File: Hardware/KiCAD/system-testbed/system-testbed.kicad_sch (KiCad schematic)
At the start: 0 parts

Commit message: Update-Jumper-Schematic
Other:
- sheet Audio Subsystem renamed Audio Subsystem (TQFN)
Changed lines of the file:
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@@
 			(color 255 229 191 1.0000)
 		)
-		(property "Sheetname" "Audio Subsystem"
+		(property "Sheetname" "Audio Subsystem (TQFN)"
 			(at 204.47 45.0084 0)
 			(effects

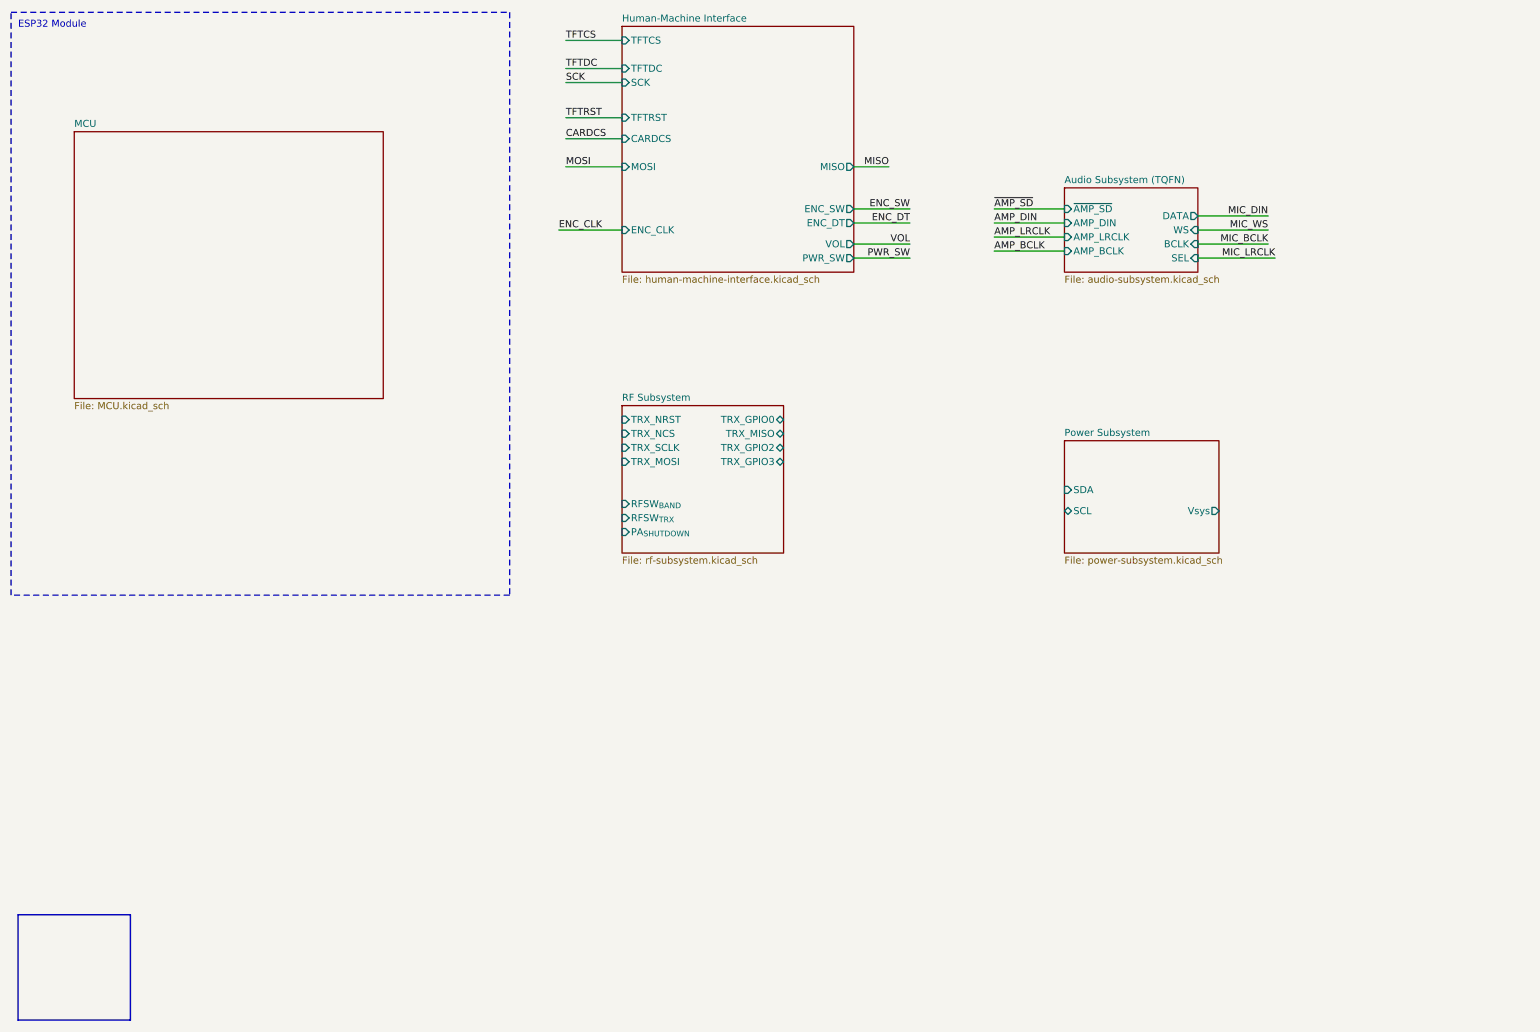
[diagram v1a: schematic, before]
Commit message: fix: clarify labellng and pin head #32
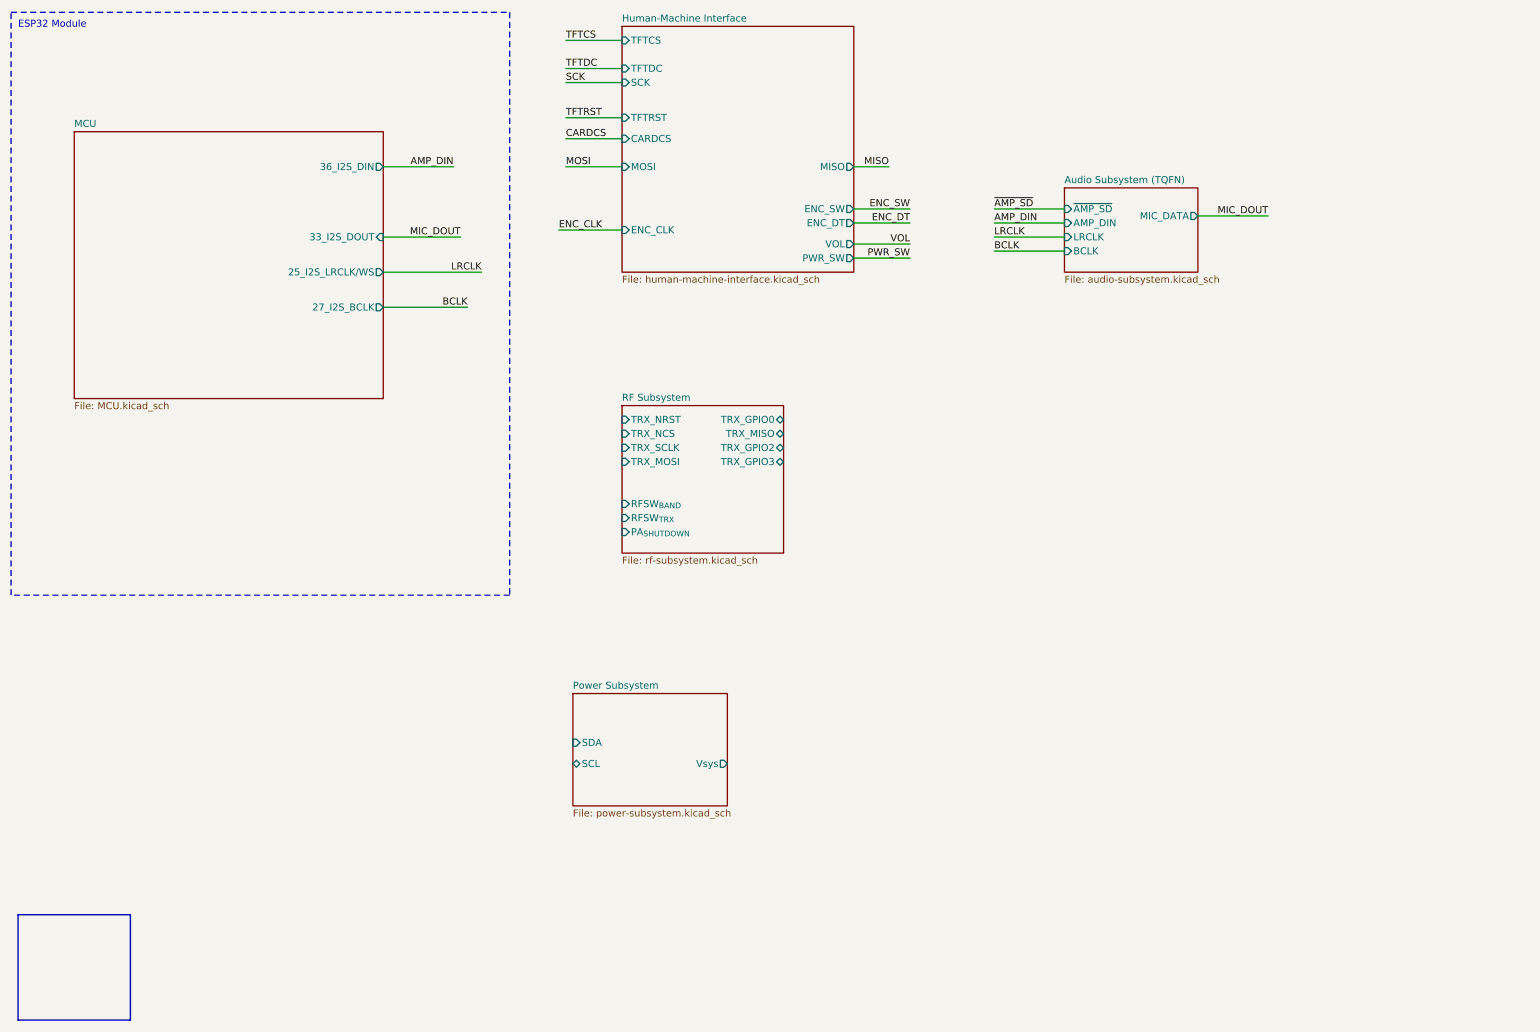
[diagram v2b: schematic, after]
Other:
- sheet Audio Subsystem (TQFN) ports: added LRCLK, MIC_DATA; removed AMP_BCLK, AMP_LRCLK, DATA, SEL, WS
- sheet MCU ports: added 25_I2S_LRCLK/WS, 27_I2S_BCLK, 33_I2S_DOUT, 36_I2S_DIN; removed none
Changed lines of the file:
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@@
 	(wire
 		(pts
-			(xy 241.3 53.34) (xy 228.6 53.34)
+			(xy 81.28 54.61) (xy 95.25 54.61)
 		)
 		(stroke
@@
 	(wire
 		(pts
-			(xy 228.6 58.42) (xy 242.57 58.42)
-		)
-		(stroke
-			(width 0)
-			(type default)
-		)
-	)
-	(wire
-		(pts
 			(xy 172.72 41.91) (xy 166.37 41.91)
 		)
@@
 	(wire
 		(pts
-			(xy 241.3 55.88) (xy 228.6 55.88)
-		)
-		(stroke
-			(width 0)
-			(type default)
-		)
-	)
-	(wire
-		(pts
 			(xy 166.37 49.53) (xy 176.53 49.53)
 		)
@@
 	(wire
 		(pts
+			(xy 81.28 60.96) (xy 99.06 60.96)
+		)
+		(stroke
+			(width 0)
+			(type default)
+		)
+	)
+	(wire
+		(pts
 			(xy 114.3 36.83) (xy 124.46 36.83)
 		)
@@
 	(wire
 		(pts
+			(xy 93.98 41.91) (xy 81.28 41.91)
+		)
+		(stroke
+			(width 0)
+			(type default)
+		)
+	)
+	(wire
+		(pts
 			(xy 114.3 24.13) (xy 124.46 24.13)
+		)
+		(stroke
+			(width 0)
+			(type default)
+		)
+	)
+	(wire
+		(pts
+			(xy 81.28 67.31) (xy 96.52 67.31)
 		)
 		(stroke
@@
 		)
 	)
-	(label "AMP_BCLK"
+	(label "BCLK"
 		(at 191.77 57.15 0)
 		(effects
@@
 			)
 			(justify left bottom)
+		)
+	)
+	(label "LRCLK"
+		(at 99.06 60.96 180)
+		(effects
+			(font
+				(size 1.27 1.27)
+			)
+			(justify right bottom)
 		)
 	)
@@
 		)
 	)
-	(label "MIC_LRCLK"
-		(at 242.57 58.42 180)
+	(label "AMP_DIN"
+		(at 93.98 41.91 180)
 		(effects
 			(font
@@
 		)
 	)
+	(label "MIC_DOUT"
+		(at 95.25 54.61 180)
+		(effects
+			(font
+				(size 1.27 1.27)
+			)
+			(justify right bottom)
+		)
+	)
 	(label "PWR_SW"
 		(at 176.53 58.42 180)
@@
 		)
 	)
-	(label "MIC_BCLK"
-		(at 241.3 55.88 180)
-		(effects
-			(font
-				(size 1.27 1.27)
-			)
-			(justify right bottom)
-		)
-	)
-	(label "MIC_DIN"
+	(label "MIC_DOUT"
 		(at 241.3 50.8 180)
 		(effects
@@
 		)
 	)
-	(label "MIC_WS"
-		(at 241.3 53.34 180)
-		(effects
-			(font
-				(size 1.27 1.27)
-			)
-			(justify right bottom)
-		)
-	)
-	(label "AMP_LRCLK"
+	(label "BCLK"
+		(at 96.52 67.31 180)
+		(effects
+			(font
+				(size 1.27 1.27)
+			)
+			(justify right bottom)
+		)
+	)
+	(label "LRCLK"
 		(at 191.77 54.61 0)
 		(effects
@@
 			)
 		)
+		(pin "36_I2S_DIN" output
+			(at 81.28 41.91 0)
+			(effects
+				(font
+					(size 1.27 1.27)
+				)
+				(justify right)
+			)
+		)
+		(pin "33_I2S_DOUT" input
+			(at 81.28 54.61 0)
+			(effects
+				(font
+					(size 1.27 1.27)
+				)
+				(justify right)
+			)
+		)
+		(pin "25_I2S_LRCLK{slash}WS" output
+			(at 81.28 60.96 0)
+			(effects
+				(font
+					(size 1.27 1.27)
+				)
+				(justify right)
+			)
+		)
+		(pin "27_I2S_BCLK" output
+			(at 81.28 67.31 0)
+			(effects
+				(font
+					(size 1.27 1.27)
+				)
+				(justify right)
+			)
+		)
 		(instances
 			(project "system-testbed"
@@
 	)
 	(sheet
-		(at 204.47 91.44)
+		(at 115.57 137.16)
 		(size 27.94 20.32)
 		(exclude_from_sim no)
@@
 		)
 		(property "Sheetname" "Power Subsystem"
-			(at 204.47 90.7284 0)
+			(at 115.57 136.4484 0)
 			(effects
 				(font
@@
 		)
 		(property "Sheetfile" "power-subsystem.kicad_sch"
-			(at 204.47 112.3446 0)
+			(at 115.57 158.0646 0)
 			(effects
 				(font
@@
 		)
 		(pin "Vsys" output
-			(at 232.41 104.14 0)
+			(at 143.51 149.86 0)
 			(effects
 				(font
@@
 		)
 		(pin "SDA" input
-			(at 204.47 100.33 180)
+			(at 115.57 146.05 180)
 			(effects
 				(font
@@
 		)
 		(pin "SCL" bidirectional
-			(at 204.47 104.14 180)
+			(at 115.57 149.86 180)
 			(effects
 				(font
@@
 			)
 		)
-		(pin "AMP_LRCLK" input
-			(at 204.47 54.61 180)
-			(effects
-				(font
-					(size 1.27 1.27)
-				)
-				(justify left)
-			)
-		)
 		(pin "~{AMP_SD}" input
 			(at 204.47 49.53 180)
@@
 			)
 		)
-		(pin "AMP_BCLK" input
+		(pin "MIC_DATA" output
+			(at 228.6 50.8 0)
+			(effects
+				(font
+					(size 1.27 1.27)
+				)
+				(justify right)
+			)
+		)
+		(pin "LRCLK" input
+			(at 204.47 54.61 180)
+			(effects
+				(font
+					(size 1.27 1.27)
+				)
+				(justify left)
+			)
+		)
+		(pin "BCLK" input
 			(at 204.47 57.15 180)
 			(effects
@@
 			)
 		)
-		(pin "DATA" output
-			(at 228.6 50.8 0)
-			(effects
-				(font
-					(size 1.27 1.27)
-				)
-				(justify right)
-			)
-		)
-		(pin "SEL" input
-			(at 228.6 58.42 0)
-			(effects
-				(font
-					(size 1.27 1.27)
-				)
-				(justify right)
-			)
-		)
-		(pin "WS" input
-			(at 228.6 53.34 0)
-			(effects
-				(font
-					(size 1.27 1.27)
-				)
-				(justify right)
-			)
-		)
-		(pin "BCLK" input
-			(at 228.6 55.88 0)
-			(effects
-				(font
-					(size 1.27 1.27)
-				)
-				(justify right)
-			)
-		)

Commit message: fix: rename #32
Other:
- sheet Audio Subsystem (TQFN) renamed Audio Subsystem
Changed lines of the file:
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@@
 			(color 255 229 191 1.0000)
 		)
-		(property "Sheetname" "Audio Subsystem (TQFN)"
+		(property "Sheetname" "Audio Subsystem"
 			(at 204.47 45.0084 0)
 			(effects

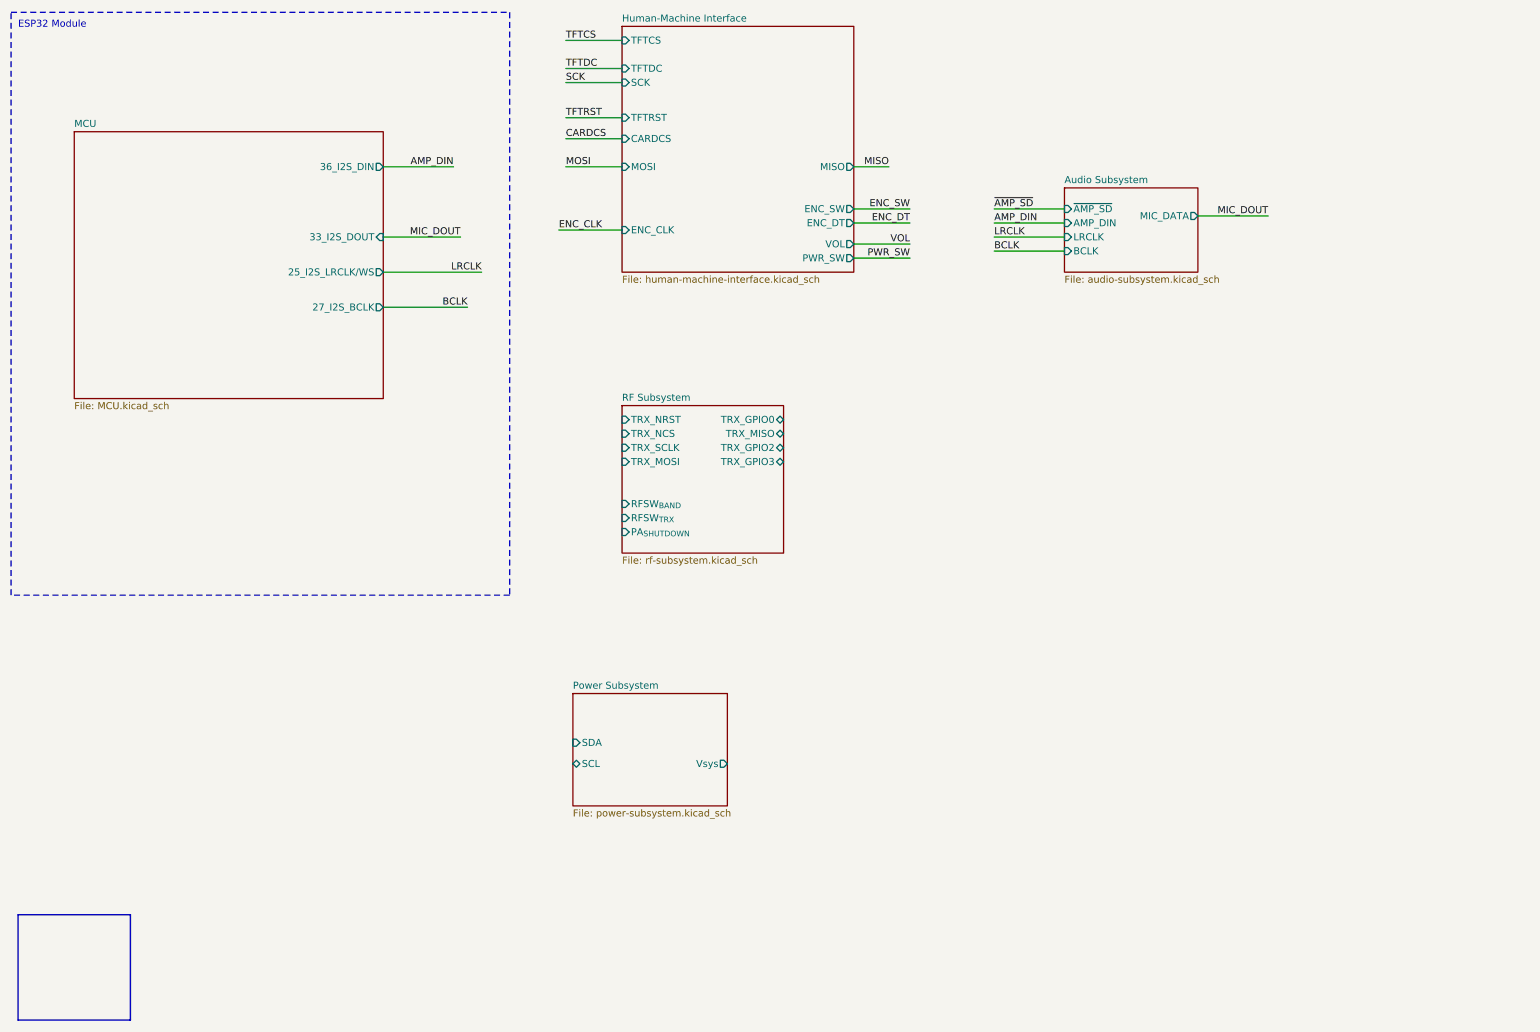
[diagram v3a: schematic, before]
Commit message: feat: move modulino interconnects to root sheet #57
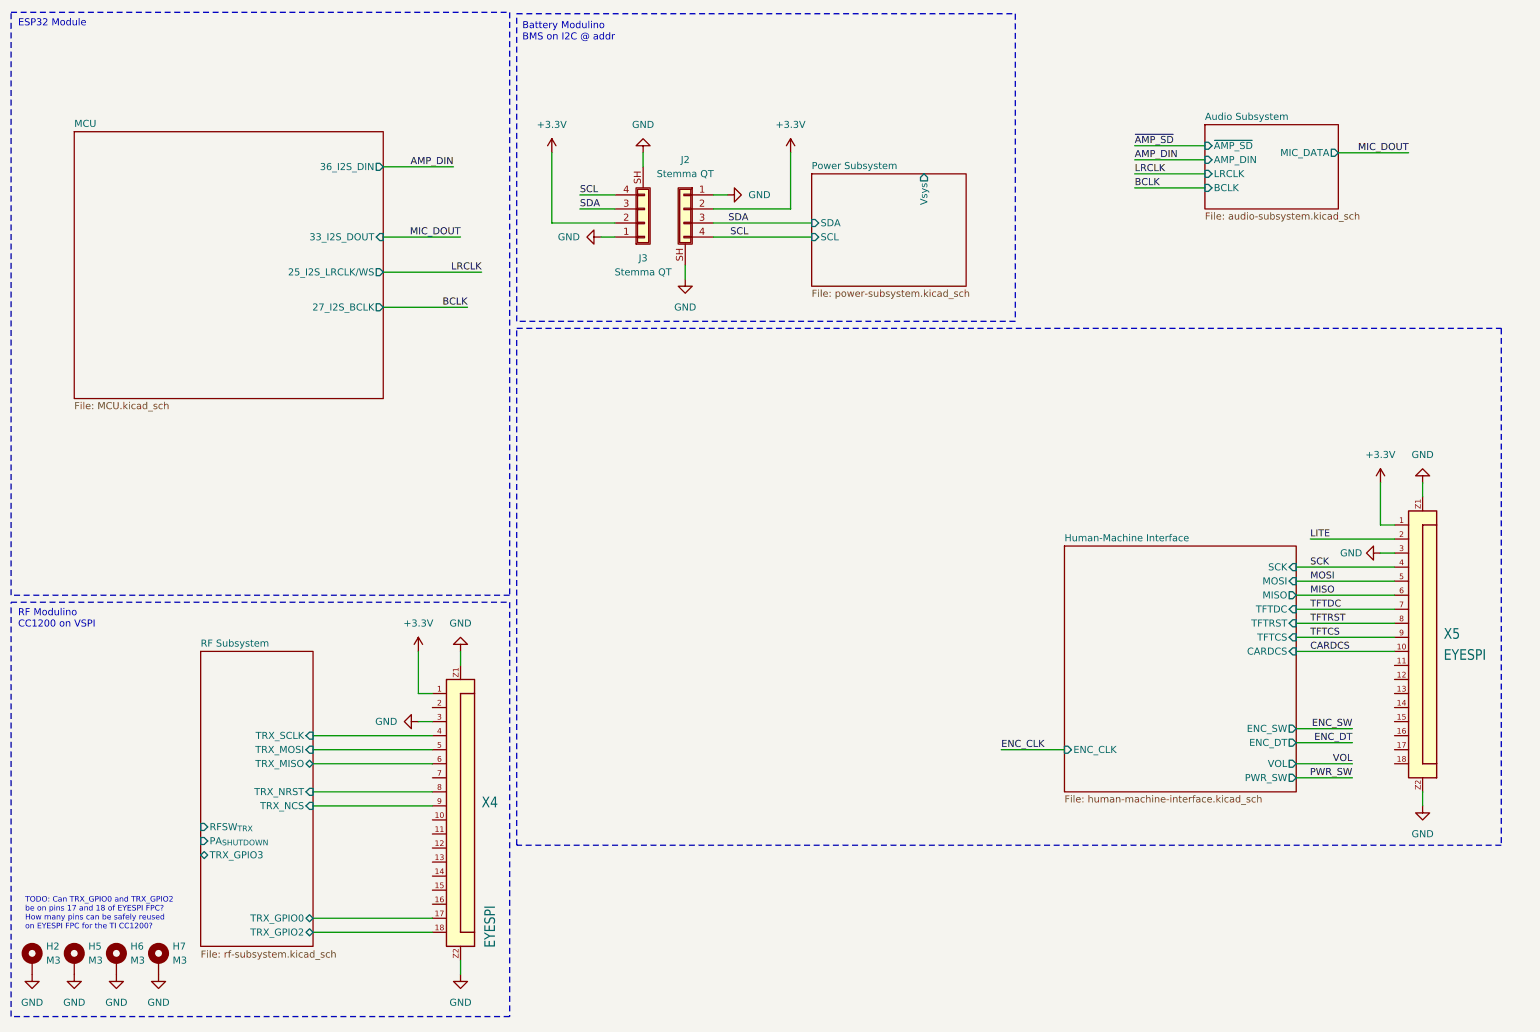
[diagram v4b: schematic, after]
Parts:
- added H2, H5, H6, H7: M3, MountingHole:MountingHole_3.2mm_M3_ISO14580_Pad, symbol Mechanical:MountingHole_Pad
- added J2, J3: Stemma QT, Connector_JST:JST_SH_SM04B-SRSS-TB_1x04-1MP_P1.00mm_Horizontal, symbol Connector_Generic_Shielded:Conn_01x04_Shielded
- added X4, X5: EYESPI, capstone-project:Adafruit EYESPI FPC Connector, symbol capstone-project:Adafruit EYESPI FPC Connector
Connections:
- net CARDCS: now also X5.10
- net MISO: now also X5.6
- net MOSI: now also X5.5
- net RF Subsystem/TRX_GPIO0: now also X4.17
- net RF Subsystem/TRX_GPIO2: now also X4.18
- net RF Subsystem/TRX_MISO: now also X4.6
- net RF Subsystem/TRX_MOSI: now also X4.5
- net RF Subsystem/TRX_NCS: now also X4.9
- net RF Subsystem/TRX_NRST: now also X4.8
- net RF Subsystem/TRX_SCLK: now also X4.4
- net SCK: now also X5.4
- net TFTCS: now also X5.9
- net TFTDC: now also X5.7
- net TFTRST: now also X5.8
- new net +3.3V: J2.2 (Pin_2), J3.2 (Pin_2), X4.1, X5.1
- new net GND: H2.1, H5.1, H6.1, H7.1, J2.1 (Pin_1), J2.SH (Shield), J3.1 (Pin_1), J3.SH (Shield), X4.3, X4.Z1, X4.Z2, X5.3, X5.Z1, X5.Z2
- new net LITE: X5.2
- new net SCL: J2.4 (Pin_4), J3.4 (Pin_4)
- new net SDA: J2.3 (Pin_3), J3.3 (Pin_3)
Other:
- sheet RF Subsystem ports: added none; removed RFSW_{BAND}
- note added: "Battery Modulino BMS on I2C @ addr"
- note added: "RF Modulino CC1200 on VSPI"
- note added: "TODO: Can TRX_GPIO0 and TRX_GPIO2 be on pins 17 and 18 of EYESPI FPC? How many pins can be safely reused on EYESPI FPC for the TI CC1200?"

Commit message: feat: schematic capture #63
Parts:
- added J4: Stemma QT, Connector_JST:JST_SH_SM04B-SRSS-TB_1x04-1MP_P1.00mm_Horizontal, symbol Connector_Generic_Shielded:Conn_01x04_Shielded
- added X6: EYESPI, capstone-project:Adafruit EYESPI FPC Connector, symbol capstone-project:Adafruit EYESPI FPC Connector
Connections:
- net +3.3V: now also J4.2 (Pin_2)
- net GND: now also J4.1 (Pin_1), J4.SH (Shield)
- net SCL: now also J4.4 (Pin_4)
- net SDA: now also J4.3 (Pin_3)
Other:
- moved on the sheet: J2, J3
